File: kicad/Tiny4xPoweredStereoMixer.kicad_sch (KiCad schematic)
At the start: 19 parts, among them J1 RCJ-2221, J2 RCJ-2221, J3 RCJ-2221, J4 RCJ-2221, J5 RCJ-2221, J6 PowerConnector, J7 PowerConnector, J8 PowerConnector, U6 LM2611AMF/NOPB

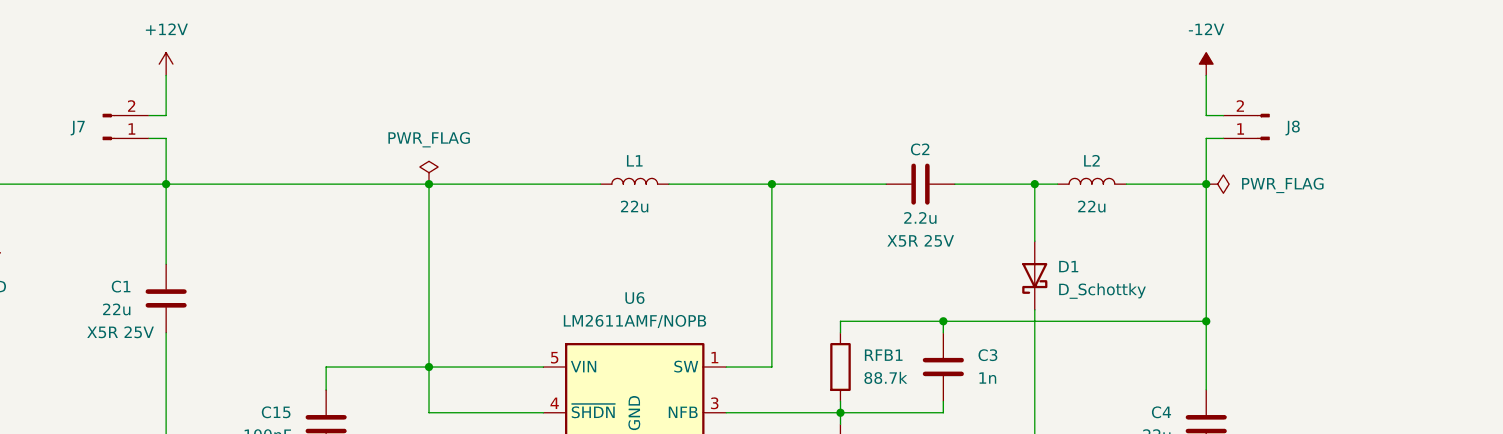
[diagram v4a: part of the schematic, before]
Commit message: updated powerflags
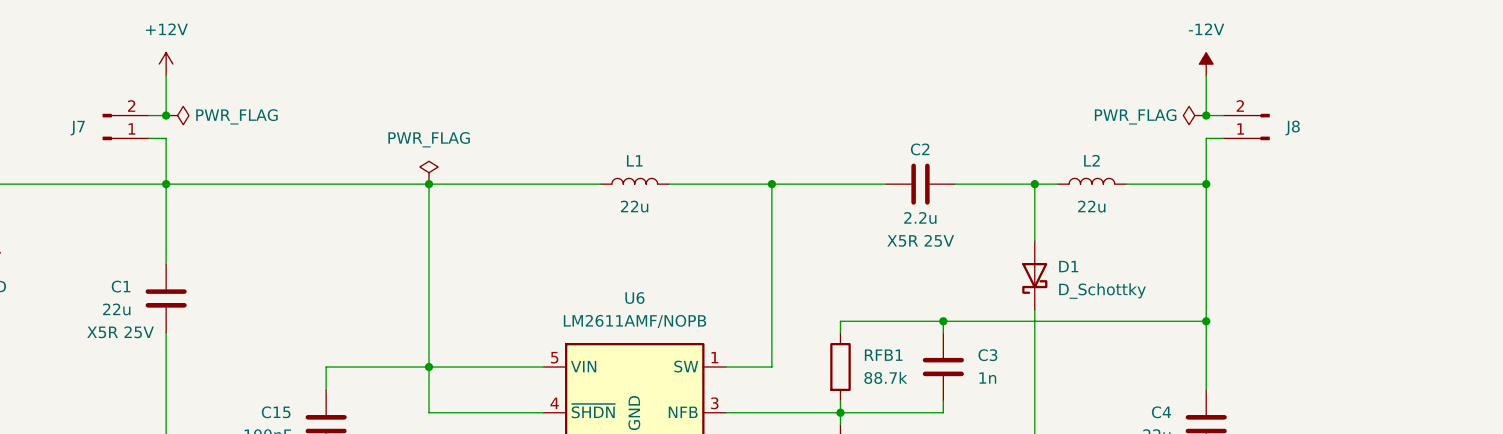
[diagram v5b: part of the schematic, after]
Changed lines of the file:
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@@
   (junction (at 62.23 78.74) (diameter 0) (color 0 0 0 0)
+  )
+  (junction (at 62.23 35.56) (diameter 0) (color 0 0 0 0)
+  )
+  (junction (at 177.8 35.56) (diameter 0) (color 0 0 0 0)
   )
   (junction (at 158.75 43.18) (diameter 0) (color 0 0 0 0)
@@
     )
   )
-  (symbol (lib_id "power:PWR_FLAG") (at 177.8 43.18 270) (unit 1)
-    (in_bom yes) (on_board yes) (dnp no) (fields_autoplaced)
-    (property "Reference" "#FLG03" (at 179.705 43.18 0)
-      (effects (font (size 1.27 1.27)) hide)
-    )
-    (property "Value" "PWR_FLAG" (at 181.61 43.18 90)
+  (symbol (lib_id "power:PWR_FLAG") (at 91.44 43.18 0) (unit 1)
+    (in_bom yes) (on_board yes) (dnp no) (fields_autoplaced)
+    (property "Reference" "#FLG04" (at 91.44 41.275 0)
+      (effects (font (size 1.27 1.27)) hide)
+    )
+    (property "Value" "PWR_FLAG" (at 91.44 38.1 0)
+      (effects (font (size 1.27 1.27)))
+    )
+    (property "Footprint" "" (at 91.44 43.18 0)
+      (effects (font (size 1.27 1.27)) hide)
+    )
+    (property "Datasheet" "~" (at 91.44 43.18 0)
+      (effects (font (size 1.27 1.27)) hide)
+    )
+    (pin "1")
+    (instances
+      (project "Tiny4xPoweredStereoMixer"
+        (path "/68c4b081-ef47-4ba5-a55f-4ef66cb2b598"
+          (reference "#FLG04") (unit 1)
+        )
+      )
+    )
+  )
+  (symbol (lib_id "power:PWR_FLAG") (at 177.8 35.56 90) (unit 1)
+    (in_bom yes) (on_board yes) (dnp no) (fields_autoplaced)
+    (property "Reference" "#FLG03" (at 175.895 35.56 0)
+      (effects (font (size 1.27 1.27)) hide)
+    )
+    (property "Value" "PWR_FLAG" (at 174.625 35.56 90)
       (effects (font (size 1.27 1.27)) (justify left))
     )
-    (property "Footprint" "" (at 177.8 43.18 0)
-      (effects (font (size 1.27 1.27)) hide)
-    )
-    (property "Datasheet" "~" (at 177.8 43.18 0)
+    (property "Footprint" "" (at 177.8 35.56 0)
+      (effects (font (size 1.27 1.27)) hide)
+    )
+    (property "Datasheet" "~" (at 177.8 35.56 0)
       (effects (font (size 1.27 1.27)) hide)
     )
@@
     )
   )
-  (symbol (lib_id "power:PWR_FLAG") (at 91.44 43.18 0) (unit 1)
-    (in_bom yes) (on_board yes) (dnp no) (fields_autoplaced)
-    (property "Reference" "#FLG02" (at 91.44 41.275 0)
-      (effects (font (size 1.27 1.27)) hide)
-    )
-    (property "Value" "PWR_FLAG" (at 91.44 38.1 0)
-      (effects (font (size 1.27 1.27)))
-    )
-    (property "Footprint" "" (at 91.44 43.18 0)
-      (effects (font (size 1.27 1.27)) hide)
-    )
-    (property "Datasheet" "~" (at 91.44 43.18 0)
-      (effects (font (size 1.27 1.27)) hide)
-    )
+  (symbol (lib_id "power:PWR_FLAG") (at 62.23 35.56 270) (unit 1)
+    (in_bom yes) (on_board yes) (dnp no) (fields_autoplaced)
+    (property "Reference" "#FLG02" (at 64.135 35.56 0)
+      (effects (font (size 1.27 1.27)) hide)
+    )
+    (property "Value" "PWR_FLAG" (at 65.405 35.56 90)
+      (effects (font (size 1.27 1.27)) (justify left))
+    )
+    (property "Footprint" "" (at 62.23 35.56 0)
+      (effects (font (size 1.27 1.27)) hide)
+    )
+    (property "Datasheet" "~" (at 62.23 35.56 0)
+      (effects (font (size 1.27 1.27)) hide)
+    )

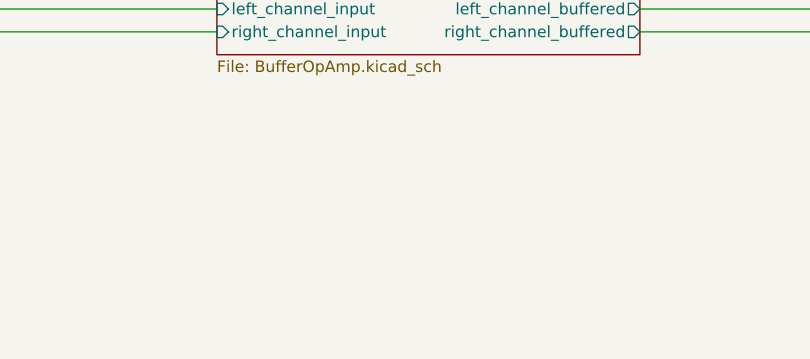
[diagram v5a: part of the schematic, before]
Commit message: add mount holes
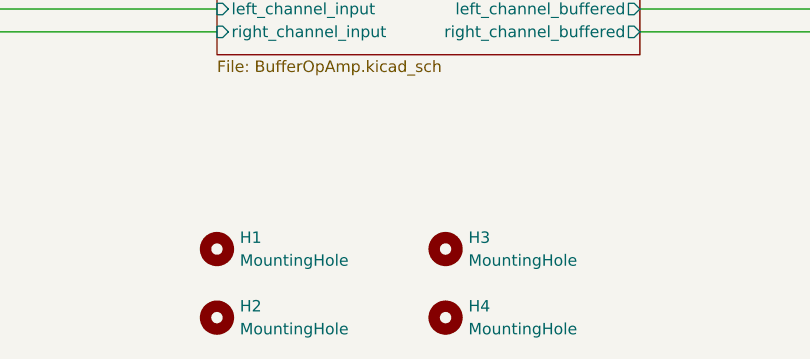
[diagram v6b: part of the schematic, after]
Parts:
- added H1, H2, H3, H4: MountingHole, MountingHole:MountingHole_4.3mm_M4_Pad, symbol Mechanical:MountingHole
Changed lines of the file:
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@@
+    )
+  )
+  (symbol (lib_id "Mechanical:MountingHole") (at 101.6 177.8 0) (unit 1)
+    (in_bom yes) (on_board yes) (dnp no) (fields_autoplaced)
+    (property "Reference" "H3" (at 104.14 176.53 0)
+      (effects (font (size 1.27 1.27)) (justify left))
+    )
+    (property "Value" "MountingHole" (at 104.14 179.07 0)
+      (effects (font (size 1.27 1.27)) (justify left))
+    )
+    (property "Footprint" "MountingHole:MountingHole_4.3mm_M4_Pad" (at 101.6 177.8 0)
+      (effects (font (size 1.27 1.27)) hide)
+    )
+    (property "Datasheet" "~" (at 101.6 177.8 0)
+      (effects (font (size 1.27 1.27)) hide)
+    )
+    (instances
+      (project "Tiny4xPoweredStereoMixer"
+        (path "/68c4b081-ef47-4ba5-a55f-4ef66cb2b598"
+          (reference "H3") (unit 1)
+        )
+      )
+    )
+  )
+  (symbol (lib_id "Mechanical:MountingHole") (at 101.6 185.42 0) (unit 1)
+    (in_bom yes) (on_board yes) (dnp no) (fields_autoplaced)
+    (property "Reference" "H4" (at 104.14 184.15 0)
+      (effects (font (size 1.27 1.27)) (justify left))
+    )
+    (property "Value" "MountingHole" (at 104.14 186.69 0)
+      (effects (font (size 1.27 1.27)) (justify left))
+    )
+    (property "Footprint" "MountingHole:MountingHole_4.3mm_M4_Pad" (at 101.6 185.42 0)
+      (effects (font (size 1.27 1.27)) hide)
+    )
+    (property "Datasheet" "~" (at 101.6 185.42 0)
+      (effects (font (size 1.27 1.27)) hide)
+    )
+    (instances
+      (project "Tiny4xPoweredStereoMixer"
+        (path "/68c4b081-ef47-4ba5-a55f-4ef66cb2b598"
+          (reference "H4") (unit 1)
+        )
+      )
     )
   )
@@
         (path "/68c4b081-ef47-4ba5-a55f-4ef66cb2b598"
           (reference "#FLG03") (unit 1)
+        )
+      )
+    )
+  )
+  (symbol (lib_id "Mechanical:MountingHole") (at 76.2 185.42 0) (unit 1)
+    (in_bom yes) (on_board yes) (dnp no) (fields_autoplaced)
+    (property "Reference" "H2" (at 78.74 184.15 0)
+      (effects (font (size 1.27 1.27)) (justify left))
+    )
+    (property "Value" "MountingHole" (at 78.74 186.69 0)
+      (effects (font (size 1.27 1.27)) (justify left))
+    )
+    (property "Footprint" "MountingHole:MountingHole_4.3mm_M4_Pad" (at 76.2 185.42 0)
+      (effects (font (size 1.27 1.27)) hide)
+    )
+    (property "Datasheet" "~" (at 76.2 185.42 0)
+      (effects (font (size 1.27 1.27)) hide)
+    )
+    (instances
+      (project "Tiny4xPoweredStereoMixer"
+        (path "/68c4b081-ef47-4ba5-a55f-4ef66cb2b598"
+          (reference "H2") (unit 1)
         )
       )
@@
         )
       )
+    )
+  )
+  (symbol (lib_id "Mechanical:MountingHole") (at 76.2 177.8 0) (unit 1)
+    (in_bom yes) (on_board yes) (dnp no) (fields_autoplaced)
+    (property "Reference" "H1" (at 78.74 176.53 0)
+      (effects (font (size 1.27 1.27)) (justify left))
+    )
+    (property "Value" "MountingHole" (at 78.74 179.07 0)
+      (effects (font (size 1.27 1.27)) (justify left))
+    )
+    (property "Footprint" "MountingHole:MountingHole_4.3mm_M4_Pad" (at 76.2 177.8 0)
+      (effects (font (size 1.27 1.27)) hide)
+    )
+    (property "Datasheet" "~" (at 76.2 177.8 0)
+      (effects (font (size 1.27 1.27)) hide)
+    )
+    (instances
+      (project "Tiny4xPoweredStereoMixer"
+        (path "/68c4b081-ef47-4ba5-a55f-4ef66cb2b598"
+          (reference "H1") (unit 1)
+        )
+      )

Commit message: completed reva layout
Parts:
- C1, C4: Mouser (none) -> 187-CL32A226KAJNNNE
- C15: Mouser (none) -> 791-0603B104J250CT
- C2: Mouser (none) -> 581-12103D225K
- C3: Mouser (none) -> 187-CL21B102JCANNNC
- D1: Mouser (none) -> 863-MBRM120LT1G
- H1, H2, H3, H4: footprint MountingHole:MountingHole_4.3mm_M4_Pad -> MountingHole:MountingHole_3mm
- J1, J2, J3, J4, J5: footprint RCAJack:RCJ-22 -> RCAJack:CUI_DEVICES_RCJ-2211
- L1, L2: Mouser (none) -> 815-ASPI-4020S-220MT
- RFB1: Mouser (none) -> 652-CR0805FX-8872ELF
- RFB2: Mouser (none) -> 71-CRCW080510K0FKEAC
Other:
- moved on the sheet: J7, J8

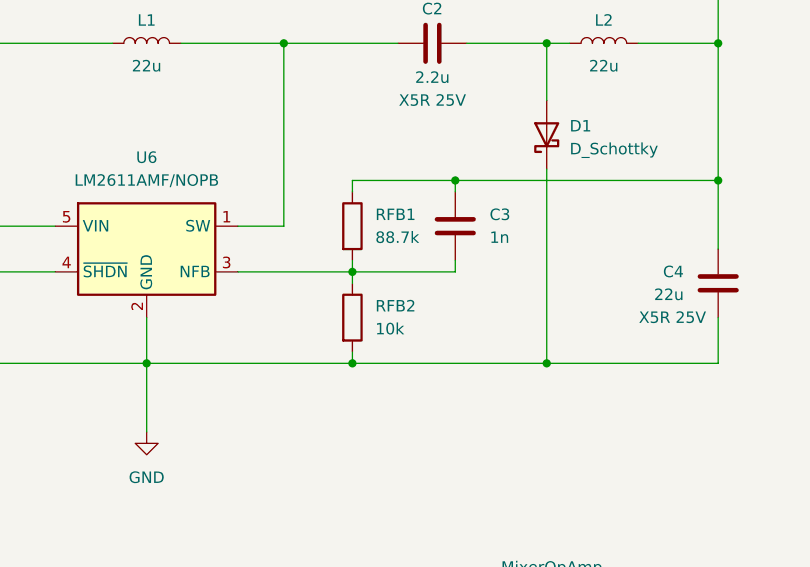
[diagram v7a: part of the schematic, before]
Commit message: updated cuk converter negative feedback resistors
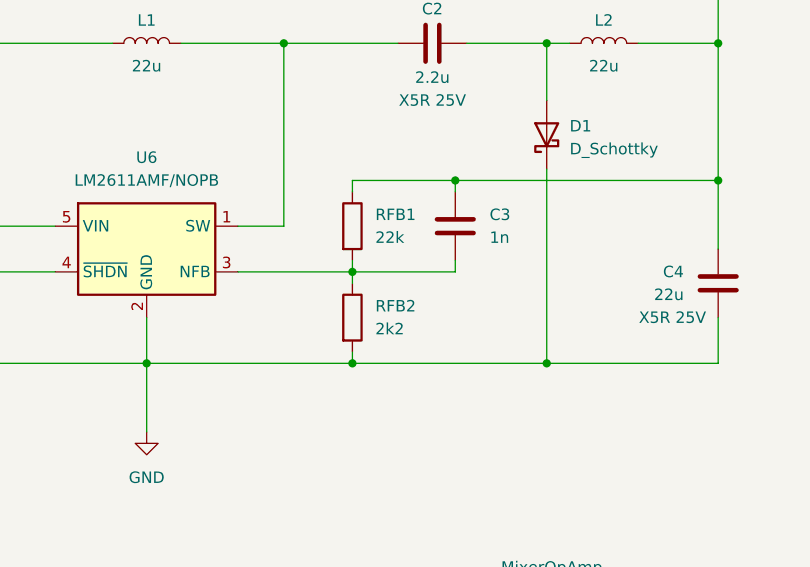
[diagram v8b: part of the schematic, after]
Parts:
- RFB1: value 88.7k -> 22k
- RFB2: value 10k -> 2k2
